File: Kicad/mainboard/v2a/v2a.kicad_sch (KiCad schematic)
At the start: 16 parts, among them U1 65c02

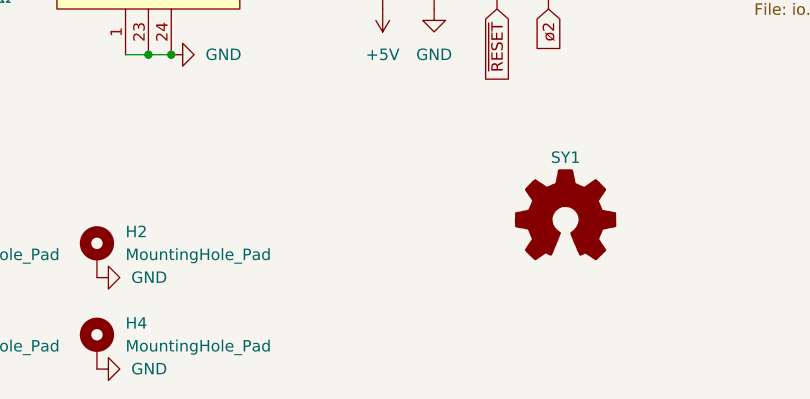
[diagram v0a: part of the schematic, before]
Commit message: Updated pcb files and python scripts
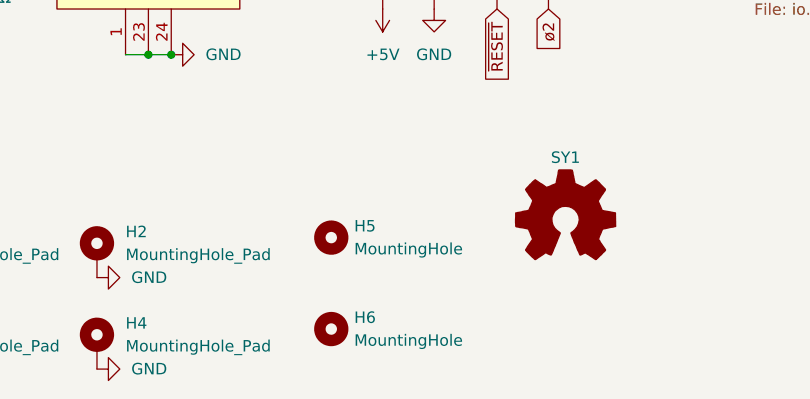
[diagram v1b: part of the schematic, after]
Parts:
- added H5, H6: MountingHole, MountingHole:MountingHole_2.2mm_M2, symbol Mechanical:MountingHole
- U1: footprint PCM_Package_LCC_AKL:PLCC-44_THT-Socket -> Smal:PLCC-44_THT-Socket_TWEAK
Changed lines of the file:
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@@
 			)
 		)
-		(property "Footprint" "PCM_Package_LCC_AKL:PLCC-44_THT-Socket"
+		(property "Footprint" "Smal:PLCC-44_THT-Socket_TWEAK"
 			(at 50.8 3.81 0)
 			(effects
@@
 					(unit 1)
 				)
+			)
+		)
+	)
+	(symbol
+		(lib_id "Mechanical:MountingHole")
+		(at 71.12 124.46 0)
+		(unit 1)
+		(exclude_from_sim yes)
+		(in_bom no)
+		(on_board yes)
+		(dnp no)
+		(fields_autoplaced yes)
+		(property "Reference" "H6"
+			(at 73.66 123.1899 0)
+			(effects
+				(font
+					(size 1.27 1.27)
+				)
+				(justify left)
+			)
+		)
+		(property "Value" "MountingHole"
+			(at 73.66 125.7299 0)
+			(effects
+				(font
+					(size 1.27 1.27)
+				)
+				(justify left)
+			)
+		)
+		(property "Footprint" "MountingHole:MountingHole_2.2mm_M2"
+			(at 71.12 124.46 0)
+			(effects
+				(font
+					(size 1.27 1.27)
+				)
+				(hide yes)
+			)
+		)
+		(property "Datasheet" "~"
+			(at 71.12 124.46 0)
+			(effects
+				(font
+					(size 1.27 1.27)
+				)
+				(hide yes)
+			)
+		)
+		(property "Description" "Mounting Hole without connection"
+			(at 71.12 124.46 0)
+			(effects
+				(font
+					(size 1.27 1.27)
+				)
+				(hide yes)
+			)
+		)
+		(instances
+			(project "v2a"
+				(path "/82bc3382-6295-4121-a2db-2433a00f189b"
+					(reference "H6")
+					(unit 1)
+				)
+			)
+		)
+	)
+	(symbol
+		(lib_id "Mechanical:MountingHole")
+		(at 71.12 114.3 0)
+		(unit 1)
+		(exclude_from_sim yes)
+		(in_bom no)
+		(on_board yes)
+		(dnp no)
+		(fields_autoplaced yes)
+		(property "Reference" "H5"
+			(at 73.66 113.0299 0)
+			(effects
+				(font
+					(size 1.27 1.27)
+				)
+				(justify left)
+			)
+		)
+		(property "Value" "MountingHole"
+			(at 73.66 115.5699 0)
+			(effects
+				(font
+					(size 1.27 1.27)
+				)
+				(justify left)
+			)
+		)
+		(property "Footprint" "MountingHole:MountingHole_2.2mm_M2"
+			(at 71.12 114.3 0)
+			(effects
+				(font
+					(size 1.27 1.27)
+				)
+				(hide yes)
+			)
+		)
+		(property "Datasheet" "~"
+			(at 71.12 114.3 0)
+			(effects
+				(font
+					(size 1.27 1.27)
+				)
+				(hide yes)
+			)
+		)
+		(property "Description" "Mounting Hole without connection"
+			(at 71.12 114.3 0)
+			(effects
+				(font
+					(size 1.27 1.27)
+				)
+				(hide yes)
+			)
+		)
+		(instances
+			(project ""
+				(path "/82bc3382-6295-4121-a2db-2433a00f189b"
+					(reference "H5")
+					(unit 1)
+				)
